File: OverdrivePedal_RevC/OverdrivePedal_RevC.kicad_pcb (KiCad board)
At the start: 2 copper layers, 42.5 x 30.5 mm, 56 parts, among them J1 AudioJack2-Connector, J2 Barrel_Jack, J3 Conn_01x05, J4 SW_SPST, J6 AudioJack2-Connector, U1 DG468DV_T1_E3, U10 PAM2812, U2 TL071, U3 TPS60400, U4 DG468DV_T1_E3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

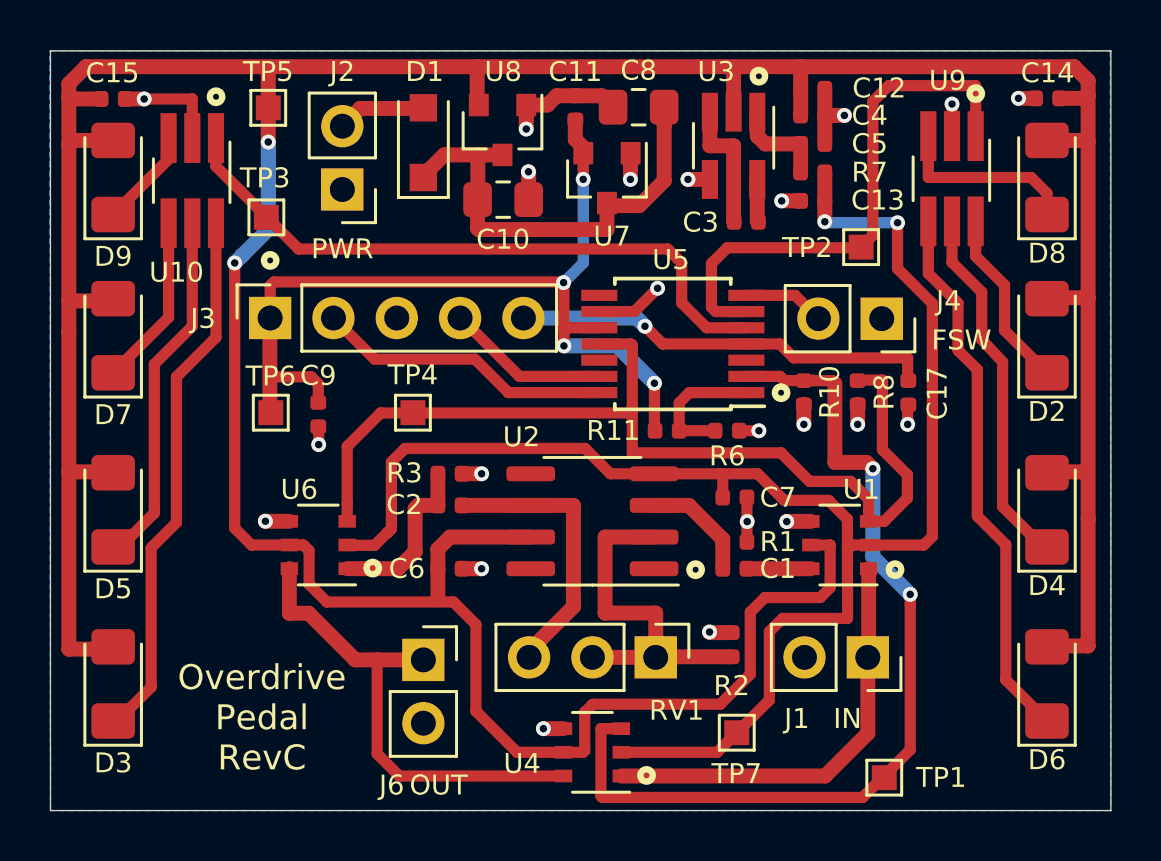
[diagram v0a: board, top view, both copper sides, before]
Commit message: updated revc
- Changed ICP header from 2.54 to 1.27
- Added trim pot connected to ADC IN7 (PA7)
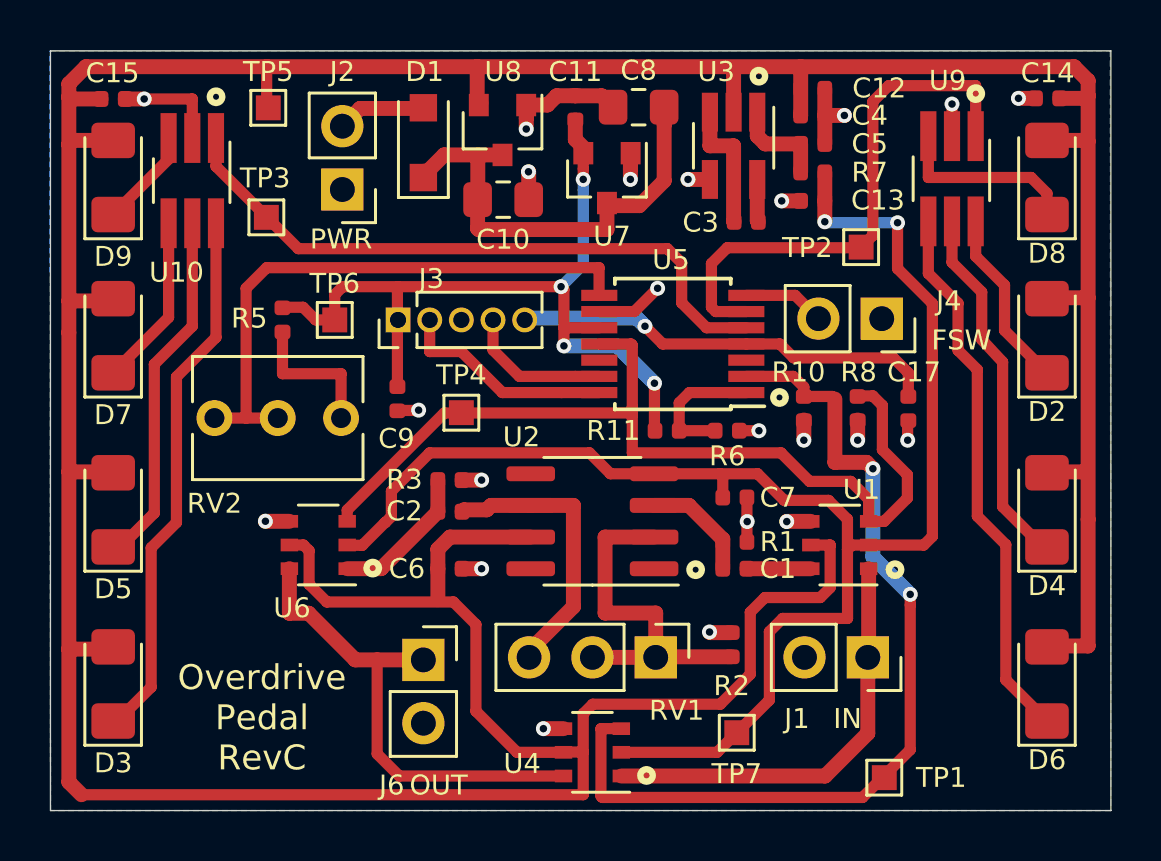
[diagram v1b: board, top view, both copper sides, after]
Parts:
- added R5: 1K, Resistor_SMD:R_0402_1005Metric, F.Cu at (132.5, 91.4)
- added RV2: B10K, Potentiometer_THT:Potentiometer_Vishay_T73XW_Horizontal, F.Cu at (129.8, 95.4)
- J3: footprint Connector_PinSocket_2.54mm:PinSocket_1x05_P2.54mm_Vertical -> Connector_PinHeader_1.27mm:PinHeader_1x05_P1.27mm_Vertical
- moved J3 5.13 mm to (137.2, 91.4)
- moved TP6 4.52 mm to (134.6, 91.4)
- moved C9 3.24 mm to (137.1, 94.6)
- moved TP4 1.94 mm to (139.7, 95.2)
- moved C17 0.63 mm to (157.6, 95.0)
- moved R10 0.63 mm to (153.4, 95.0)
- moved R8 0.63 mm to (155.6, 95.0)
- moved C2 0.25 mm to (139.2, 99.1)
- moved R3 0.25 mm to (139.2, 97.9)
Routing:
- net Net-(RV2-Pad1): track 0.00 -> 23.4 mm
- net +5V: track 171.1 -> 179.3 mm, vias 2 -> 0
- net Net-(R5-Pad1): track 0.00 -> 5.80 mm
- net /SYS_SWCLK: track 11.9 -> 8.76 mm
- net +3V3: track 36.4 -> 33.5 mm
- net /FX_ENABLE: track 40.1 -> 37.9 mm
- net -5V: track 64.0 -> 62.9 mm
- net Net-(C2-Pad1): track 6.97 -> 5.85 mm
- net /SYS_SWDIO: track 6.55 -> 5.91 mm
